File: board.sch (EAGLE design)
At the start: 65 parts, among them K1 FTR-K1C, K2 FTR-K1C, K3 FTR-K1C, K4 FTR-K1C, X6 PN61729-S

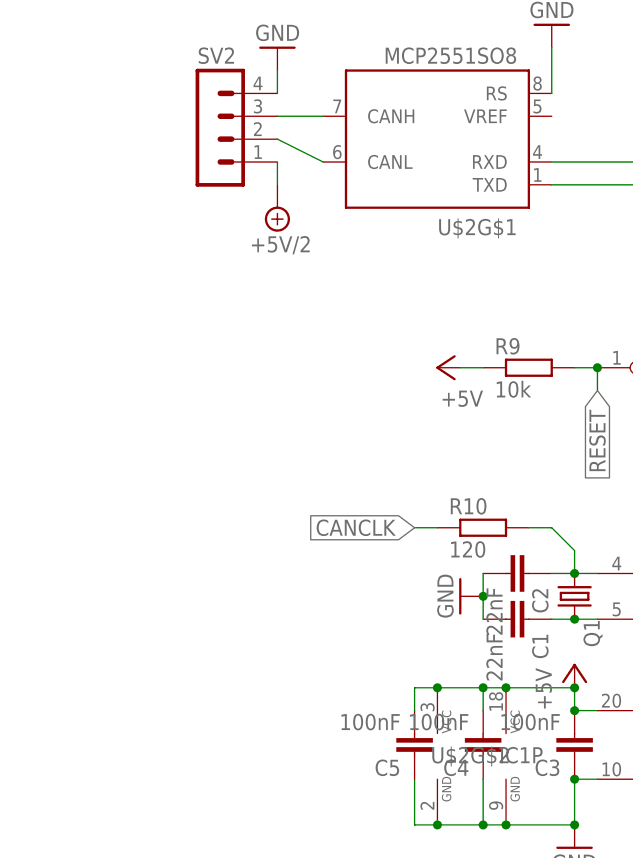
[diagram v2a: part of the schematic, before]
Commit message: Adding crappy support for a step-down voltage regulator
Well, there should be a different package for the LM2574…
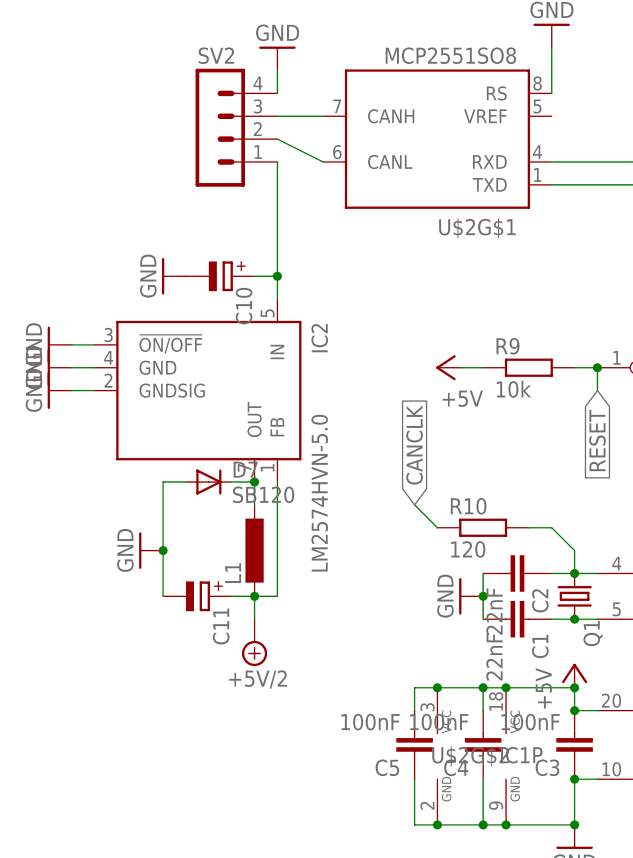
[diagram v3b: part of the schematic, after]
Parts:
- added C10, C11: (no value), rcl:CPOL-EUD
- added D7: SB120, diode:SB120
- added IC2: LM2574HVN-5.0, linear:LM2574HVN-5.0
- added L1: (no value), rcl:L-EUPIS2816
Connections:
- new net N$38: C10.+, IC2.IN, SV2.1
- new net N$8: D7.C, IC2.OUT, L1.1
- net +5V/2: now also C11.+, IC2.FB, L1.2; no longer SV2.1
- net GND: now also C10.-, C11.-, D7.A, IC2.!ON/OFF, IC2.GND@PWR, IC2.GNDSIG
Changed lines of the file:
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@@
 <part name="SV2" library="con-lstb" deviceset="MA04-1" device=""/>
 <part name="SUPPLY4" library="supply2" deviceset="+5V/2" device=""/>
+<part name="IC2" library="linear" deviceset="LM2574?-*" device="HVN" technology="5.0"/>
+<part name="GND18" library="supply1" deviceset="GND" device=""/>
+<part name="GND19" library="supply1" deviceset="GND" device=""/>
+<part name="GND20" library="supply1" deviceset="GND" device=""/>
+<part name="C10" library="rcl" deviceset="CPOL-EU" device="D"/>
+<part name="C11" library="rcl" deviceset="CPOL-EU" device="D"/>
+<part name="D7" library="diode" deviceset="SB120" device=""/>
+<part name="L1" library="rcl" deviceset="L-EU" device="PIS2816"/>
+<part name="GND21" library="supply1" deviceset="GND" device=""/>
+<part name="GND22" library="supply1" deviceset="GND" device=""/>
 </parts>
 <sheets>
@@
 <instance part="SV3" gate="G$1" x="154.94" y="25.4" rot="MR180"/>
 <instance part="SV2" gate="1" x="-33.02" y="124.46"/>
-<instance part="SUPPLY4" gate="G$1" x="-25.4" y="114.3" rot="R180"/>
+<instance part="SUPPLY4" gate="G$1" x="-27.94" y="66.04" rot="R180"/>
+<instance part="IC2" gate="G$1" x="-33.02" y="93.98" rot="R270"/>
+<instance part="GND18" gate="1" x="-50.8" y="99.06" rot="R270"/>
+<instance part="GND19" gate="1" x="-50.8" y="96.52" rot="R270"/>
+<instance part="GND20" gate="1" x="-50.8" y="93.98" rot="R270"/>
+<instance part="C10" gate="G$1" x="-30.48" y="106.68" rot="R270"/>
+<instance part="C11" gate="G$1" x="-33.02" y="71.12" rot="R270"/>
+<instance part="D7" gate="1" x="-33.02" y="83.82"/>
+<instance part="L1" gate="G$1" x="-27.94" y="76.2"/>
+<instance part="GND21" gate="1" x="-38.1" y="106.68" rot="R270"/>
+<instance part="GND22" gate="1" x="-40.64" y="76.2" rot="R270"/>
 </instances>
 <busses>
@@
 <wire x1="-25.4" y1="129.54" x2="-25.4" y2="127" width="0.1524" layer="91"/>
 </segment>
+<segment>
+<pinref part="GND18" gate="1" pin="GND"/>
+<pinref part="IC2" gate="G$1" pin="!ON/OFF"/>
+<wire x1="-48.26" y1="99.06" x2="-45.72" y2="99.06" width="0.1524" layer="91"/>
+</segment>
+<segment>
+<pinref part="IC2" gate="G$1" pin="GND@PWR"/>
+<pinref part="GND19" gate="1" pin="GND"/>
+<wire x1="-45.72" y1="96.52" x2="-48.26" y2="96.52" width="0.1524" layer="91"/>
+</segment>
+<segment>
+<pinref part="GND20" gate="1" pin="GND"/>
+<pinref part="IC2" gate="G$1" pin="GNDSIG"/>
+<wire x1="-48.26" y1="93.98" x2="-45.72" y2="93.98" width="0.1524" layer="91"/>
+</segment>
+<segment>
+<pinref part="C10" gate="G$1" pin="-"/>
+<pinref part="GND21" gate="1" pin="GND"/>
+</segment>
+<segment>
+<pinref part="C11" gate="G$1" pin="-"/>
+<pinref part="D7" gate="1" pin="A"/>
+<wire x1="-38.1" y1="71.12" x2="-38.1" y2="76.2" width="0.1524" layer="91"/>
+<wire x1="-38.1" y1="76.2" x2="-38.1" y2="83.82" width="0.1524" layer="91"/>
+<wire x1="-38.1" y1="83.82" x2="-35.56" y2="83.82" width="0.1524" layer="91"/>
+<pinref part="GND22" gate="1" pin="GND"/>
+<junction x="-38.1" y="76.2"/>
+</segment>
 </net>
 <net name="N$9" class="0">
@@
 <segment>
 <pinref part="R10" gate="G$1" pin="1"/>
-<wire x1="-7.62" y1="78.74" x2="-10.16" y2="78.74" width="0.1524" layer="91"/>
-<label x="-10.16" y="78.74" size="1.778" layer="95" rot="R180" xref="yes"/>
+<wire x1="-7.62" y1="78.74" x2="-10.16" y2="81.28" width="0.1524" layer="91"/>
+<label x="-10.16" y="81.28" size="1.778" layer="95" rot="R90" xref="yes"/>
 </segment>
 </net>
@@
 </segment>
 <segment>
+<pinref part="L1" gate="G$1" pin="2"/>
+<pinref part="C11" gate="G$1" pin="+"/>
+<wire x1="-27.94" y1="71.12" x2="-30.48" y2="71.12" width="0.1524" layer="91"/>
+<pinref part="SUPPLY4" gate="G$1" pin="+5V/2"/>
+<wire x1="-27.94" y1="71.12" x2="-27.94" y2="68.58" width="0.1524" layer="91"/>
+<junction x="-27.94" y="71.12"/>
+<pinref part="IC2" gate="G$1" pin="FB"/>
+<wire x1="-25.4" y1="83.82" x2="-25.4" y2="71.12" width="0.1524" layer="91"/>
+<wire x1="-25.4" y1="71.12" x2="-27.94" y2="71.12" width="0.1524" layer="91"/>
+</segment>
+</net>
+<net name="N$8" class="0">
+<segment>
+<pinref part="IC2" gate="G$1" pin="OUT"/>
+<pinref part="L1" gate="G$1" pin="1"/>
+<pinref part="D7" gate="1" pin="C"/>
+<wire x1="-27.94" y1="83.82" x2="-27.94" y2="81.28" width="0.1524" layer="91"/>
+<wire x1="-30.48" y1="83.82" x2="-27.94" y2="83.82" width="0.1524" layer="91"/>
+<junction x="-27.94" y="83.82"/>
+</segment>
+</net>
+<net name="N$38" class="0">
+<segment>
 <pinref part="SV2" gate="1" pin="1"/>
-<pinref part="SUPPLY4" gate="G$1" pin="+5V/2"/>
-<wire x1="-25.4" y1="116.84" x2="-25.4" y2="119.38" width="0.1524" layer="91"/>
-</segment>
-</net>
+<pinref part="C10" gate="G$1" pin="+"/>
+<wire x1="-25.4" y1="119.38" x2="-25.4" y2="106.68" width="0.1524" layer="91"/>
+<pinref part="IC2" gate="G$1" pin="IN"/>
+<wire x1="-25.4" y1="106.68" x2="-27.94" y2="106.68" width="0.1524" layer="91"/>
+<wire x1="-25.4" y1="106.68" x2="-25.4" y2="104.14" width="0.1524" layer="91"/>
+<junction x="-25.4" y="106.68"/>
+</segment>
+</net>
